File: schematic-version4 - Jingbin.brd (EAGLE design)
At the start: 47 x 28 mm, 54 parts, among them J2 FTDI_DEVICE, M1 WIRELESS-NRF24L01, Q1 8MHz, T1 NMOS, T2 NMOS, T3 NMOS, T4 NMOS, U1 ATMEGA328P_TQFP, U2 GY-521MPU6050

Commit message: Version 4 complete
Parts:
- moved U2 15.9 mm to (15.5, 15.7), turned to 270 degrees
- moved Q1 15.4 mm to (33.2, 25.2)
- moved S2 10.2 mm to (39.8, 16.9), turned to 90 degrees
- moved C15 3.86 mm to (10.4, 21.5), turned to 0 degrees
- moved R13 3.16 mm to (40.1, 10.7), flipped to the top
- moved T1 3.11 mm to (40.1, 8.15), flipped to the top
- moved D1 2.92 mm to (39.2, 5.66)
- moved C14 2.02 mm to (7.32, 21.5), turned to 0 degrees
- moved T2 1.63 mm to (35.4, 7.80)
- moved D2 1.47 mm to (32.8, 6.68)
- moved R14 1.32 mm to (35.2, 10.4)
- moved T3 0.96 mm to (29.0, 6.35)
- moved R15 0.92 mm to (28.9, 8.89)
- moved LED3 0.89 mm to (32.8, 20.5)
- moved R12 0.89 mm to (30.1, 20.4)
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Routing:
- net SDA: track 13.6 -> 51.8 mm, vias 1 -> 3
- net V_REG_OUT: track 59.7 -> 86.8 mm
- net SCL: track 14.2 -> 41.2 mm, vias 1 -> 3
- net N$1: track 6.15 -> 19.8 mm
- net N$4: track 9.91 -> 21.9 mm
- net N$2: track 22.7 -> 14.0 mm, vias 2 -> 0
- net GND: track 113.2 -> 121.2 mm
- net PWM1: track 17.8 -> 25.5 mm, vias 1 -> 2
- net PWR: track 74.2 -> 77.1 mm, vias 2 -> 1
- net DTR: track 6.91 -> 8.03 mm, vias 0 -> 1
- net PWM3: track 14.6 -> 15.6 mm
- net N$5: track 8.11 -> 7.39 mm
- net N$3: track 6.12 -> 6.83 mm, vias 0 -> 1
- net RXD: track 17.3 -> 16.6 mm, vias 2 -> 3
- net PWM2: track 19.7 -> 20.4 mm
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
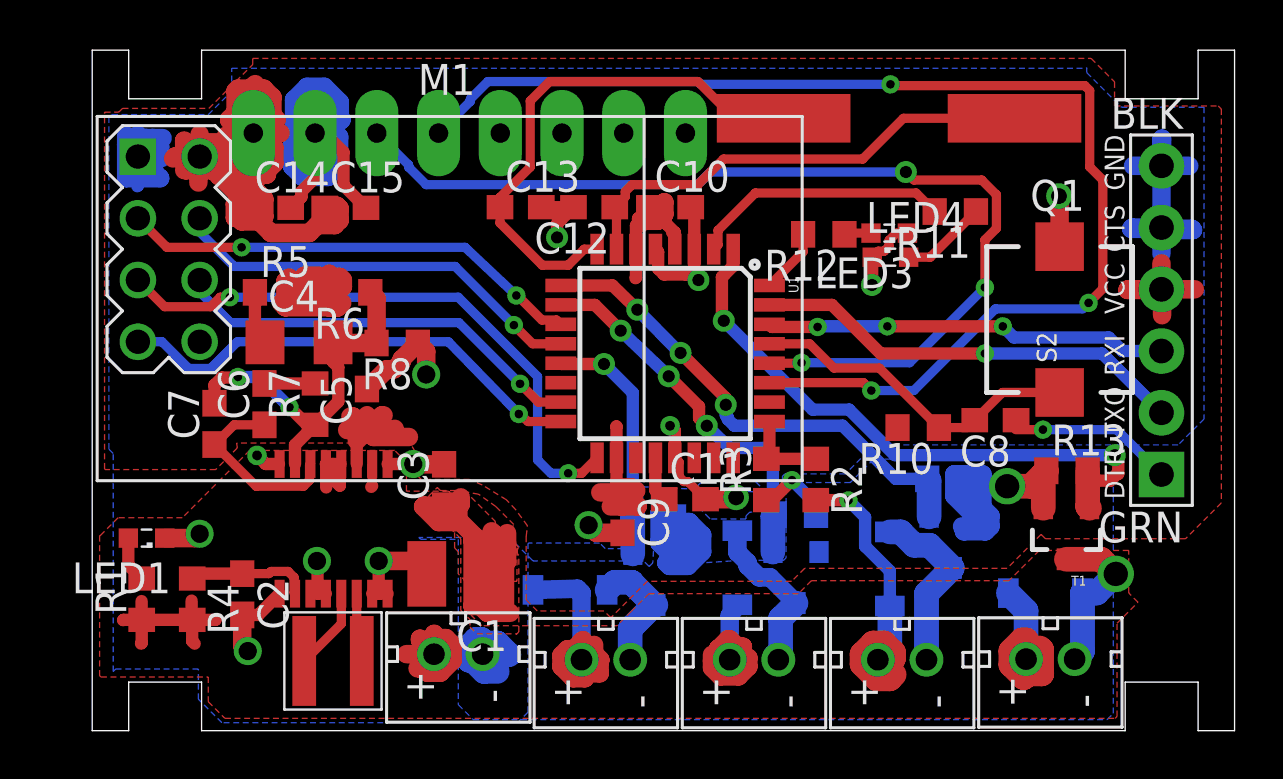
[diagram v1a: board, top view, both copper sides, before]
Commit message: More adjustments to widen some paths and ensure multiple connection
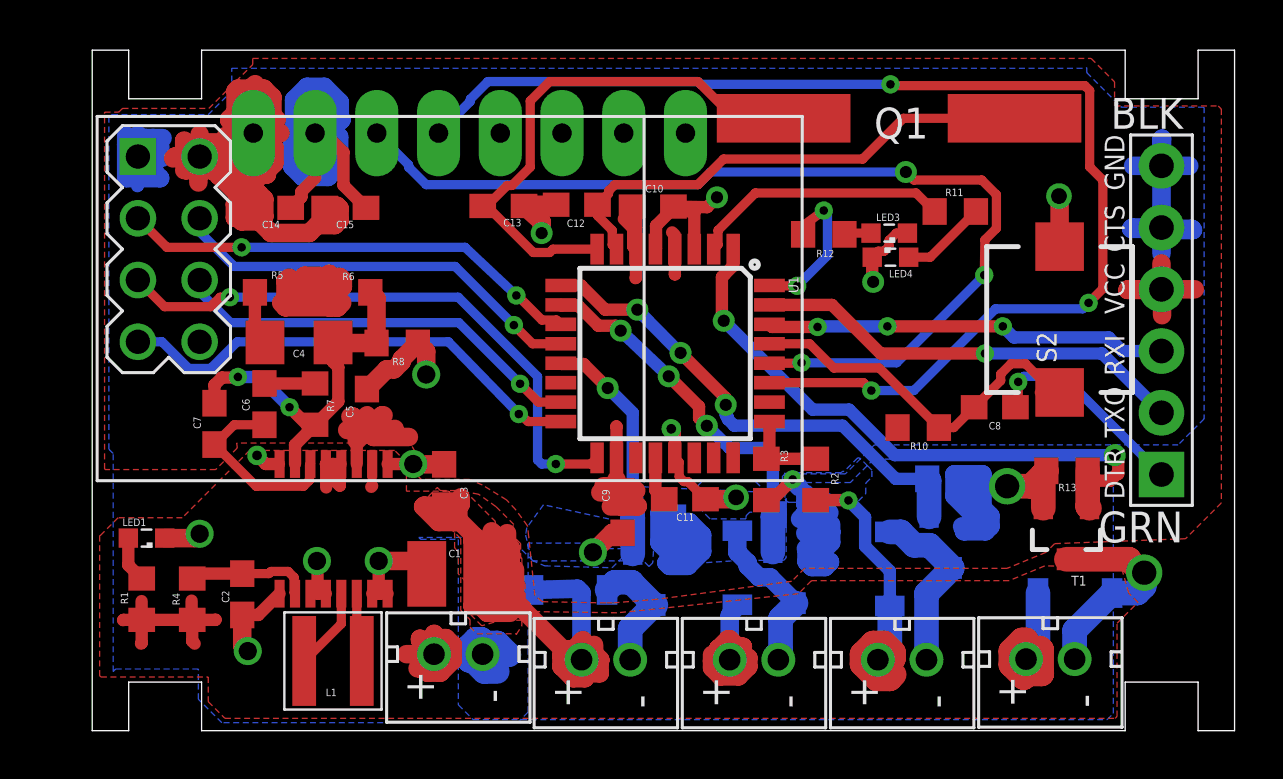
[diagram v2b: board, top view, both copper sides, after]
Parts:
- moved D1 1.22 mm to (40.5, 5.66)
- moved C12 0.72 mm to (19.9, 21.6)
- moved C13 0.71 mm to (16.9, 21.6)
- moved C10 0.71 mm to (23.1, 21.6)
- moved C8 0.53 mm to (37.1, 13.3)
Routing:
- net PWR: track 77.1 -> 86.2 mm
- net GND: track 121.2 -> 128.1 mm
- net DEBUG_LED1: track 2.68 -> 6.27 mm, vias 0 -> 2
- net N$2: track 14.0 -> 15.9 mm
- net N$3: track 6.83 -> 8.79 mm
- net N$1: track 19.8 -> 20.8 mm
- net DTR: track 8.03 -> 8.75 mm
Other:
- board text added: "L1"
